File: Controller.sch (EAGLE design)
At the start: 18 parts, among them IC1 PIC16F1826/27SO, X1 057-010-1

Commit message: Updates
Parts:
- added C3: (no value), resistor:C-EUC1206
- renumbered JP1 to CS0, JP2 to CS1, JP3 to CS2, JP4 to CS3
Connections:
- net +5V: now also C3.1
- net GND: now also C3.2
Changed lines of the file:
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@@
 <part name="SUPPLY1" library="supply2" deviceset="GND" device=""/>
 <part name="SUPPLY2" library="supply2" deviceset="+5V" device=""/>
-<part name="JP1" library="SparkFun-Jumpers" deviceset="JUMPER-SMT_2_NO" device="_SILK"/>
-<part name="JP2" library="SparkFun-Jumpers" deviceset="JUMPER-SMT_2_NO" device="_SILK"/>
-<part name="JP3" library="SparkFun-Jumpers" deviceset="JUMPER-SMT_2_NO" device="_SILK"/>
-<part name="JP4" library="SparkFun-Jumpers" deviceset="JUMPER-SMT_2_NO" device="_SILK"/>
+<part name="CS0" library="SparkFun-Jumpers" deviceset="JUMPER-SMT_2_NO" device="_SILK"/>
+<part name="CS1" library="SparkFun-Jumpers" deviceset="JUMPER-SMT_2_NO" device="_SILK"/>
+<part name="CS2" library="SparkFun-Jumpers" deviceset="JUMPER-SMT_2_NO" device="_SILK"/>
+<part name="CS3" library="SparkFun-Jumpers" deviceset="JUMPER-SMT_2_NO" device="_SILK"/>
 <part name="Q1" library="crystal" deviceset="CRYSTAL" device="HC49S"/>
 <part name="C1" library="resistor" deviceset="C-EU" device="C1206"/>
@@
 <part name="SUPPLY14" library="supply2" deviceset="GND" device=""/>
 <part name="SUPPLY15" library="supply2" deviceset="+5V" device=""/>
+<part name="SUPPLY16" library="supply2" deviceset="+5V" device=""/>
+<part name="SUPPLY17" library="supply2" deviceset="GND" device=""/>
+<part name="C3" library="resistor" deviceset="C-EU" device="C1206"/>
 </parts>
 <sheets>
@@
 <instance part="SUPPLY1" gate="GND" x="35.56" y="116.84"/>
 <instance part="SUPPLY2" gate="+5V" x="58.42" y="111.76"/>
-<instance part="JP1" gate="G$1" x="109.22" y="83.82"/>
-<instance part="JP2" gate="G$1" x="109.22" y="73.66"/>
-<instance part="JP3" gate="G$1" x="109.22" y="63.5"/>
-<instance part="JP4" gate="G$1" x="109.22" y="53.34"/>
+<instance part="CS0" gate="G$1" x="109.22" y="83.82"/>
+<instance part="CS1" gate="G$1" x="109.22" y="73.66"/>
+<instance part="CS2" gate="G$1" x="109.22" y="63.5"/>
+<instance part="CS3" gate="G$1" x="109.22" y="53.34"/>
 <instance part="Q1" gate="G$1" x="76.2" y="60.96" rot="R90"/>
 <instance part="C1" gate="G$1" x="76.2" y="55.88"/>
@@
 <instance part="SUPPLY14" gate="GND" x="-12.7" y="15.24"/>
 <instance part="SUPPLY15" gate="+5V" x="-12.7" y="38.1"/>
+<instance part="SUPPLY16" gate="+5V" x="10.16" y="83.82"/>
+<instance part="SUPPLY17" gate="GND" x="10.16" y="71.12"/>
+<instance part="C3" gate="G$1" x="10.16" y="78.74"/>
 </instances>
 <busses>
@@
 <pinref part="SUPPLY14" gate="GND" pin="GND"/>
 </segment>
+<segment>
+<pinref part="SUPPLY17" gate="GND" pin="GND"/>
+<pinref part="C3" gate="G$1" pin="2"/>
+</segment>
 </net>
 <net name="+5V" class="0">
@@
 <pinref part="SUPPLY15" gate="+5V" pin="+5V"/>
 </segment>
+<segment>
+<pinref part="SUPPLY16" gate="+5V" pin="+5V"/>
+<pinref part="C3" gate="G$1" pin="1"/>
+</segment>
 </net>
 <net name="N$1" class="0">
@@
 <net name="N$4" class="0">
 <segment>
-<pinref part="JP1" gate="G$1" pin="1"/>
-<pinref part="JP2" gate="G$1" pin="1"/>
+<pinref part="CS0" gate="G$1" pin="1"/>
+<pinref part="CS1" gate="G$1" pin="1"/>
 <wire x1="104.14" y1="83.82" x2="104.14" y2="73.66" width="0.1524" layer="91"/>
-<pinref part="JP3" gate="G$1" pin="1"/>
+<pinref part="CS2" gate="G$1" pin="1"/>
 <wire x1="104.14" y1="73.66" x2="104.14" y2="63.5" width="0.1524" layer="91"/>
 <junction x="104.14" y="73.66"/>
-<pinref part="JP4" gate="G$1" pin="1"/>
+<pinref part="CS3" gate="G$1" pin="1"/>
 <wire x1="104.14" y1="63.5" x2="104.14" y2="53.34" width="0.1524" layer="91"/>
 <junction x="104.14" y="63.5"/>
@@
 <net name="N$5" class="0">
 <segment>
-<pinref part="JP1" gate="G$1" pin="2"/>
+<pinref part="CS0" gate="G$1" pin="2"/>
 <pinref part="X1" gate="-2" pin="S"/>
 </segment>
@@
 <net name="N$6" class="0">
 <segment>
-<pinref part="JP2" gate="G$1" pin="2"/>
+<pinref part="CS1" gate="G$1" pin="2"/>
 <pinref part="X1" gate="-4" pin="S"/>
 </segment>
@@
 <net name="N$7" class="0">
 <segment>
-<pinref part="JP3" gate="G$1" pin="2"/>
+<pinref part="CS2" gate="G$1" pin="2"/>
 <pinref part="X1" gate="-8" pin="S"/>
 </segment>
@@
 <net name="N$8" class="0">
 <segment>
-<pinref part="JP4" gate="G$1" pin="2"/>
+<pinref part="CS3" gate="G$1" pin="2"/>
 <pinref part="X1" gate="-10" pin="S"/>
 </segment>

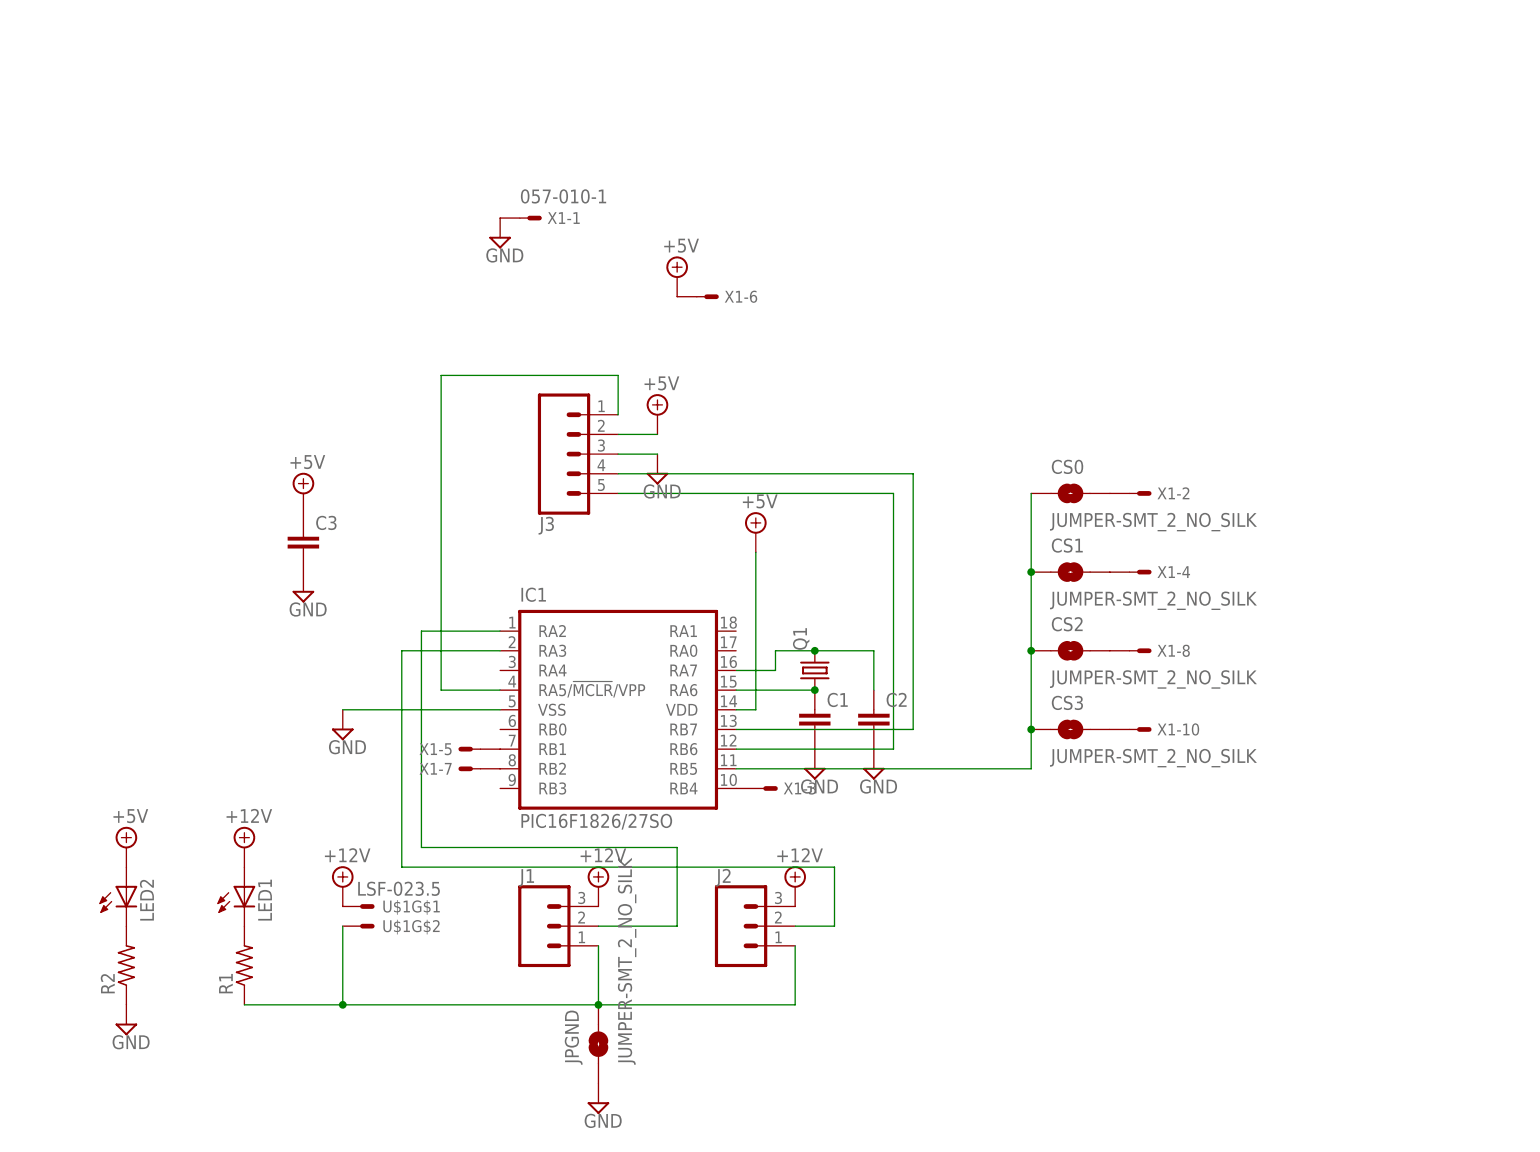
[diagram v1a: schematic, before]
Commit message: Updated design to include 5V power supply
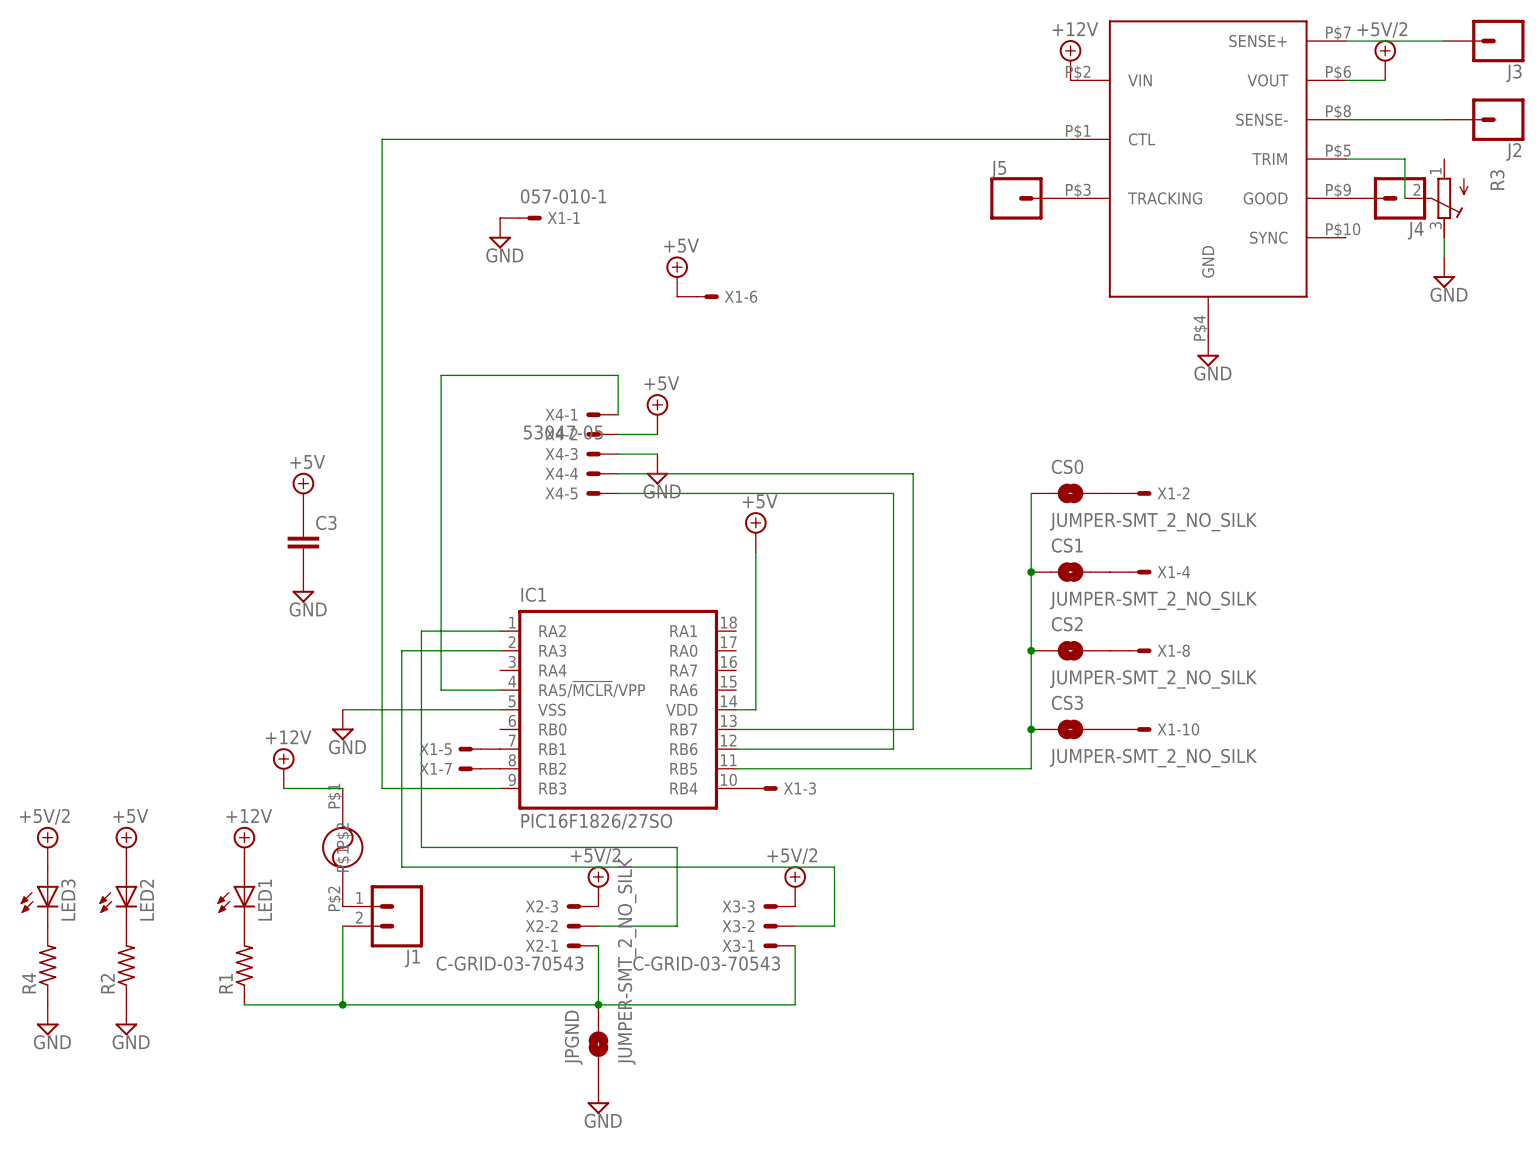
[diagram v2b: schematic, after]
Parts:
- removed C1, C2: (no value), resistor:C-EUC1206
- removed Q1: (no value), crystal:CRYSTALHC49S
- removed U$1: LSF-023.5, FRC696:LSF-023.5
- added J4, J5: (no value), SparkFun-Connectors:CONN_01
- added LED3: (no value), led:LEDCHIPLED_1206
- added R3: (no value), resistor:R-TRIMM4G/J
- added R4: (no value), resistor:R-US_R1206
- added U$2: OKL2-T12-W12, FRC696:OKL2-T12-W12
- added U$3: 0034.6081, JSB2:0034.6081
- added X2, X3: C-GRID-03-70543, con-molex:C-GRID-03-70543
- added X4: 53047-05, con-molex:53047-05
- J1: device SparkFun-Connectors:CONN_03 -> SparkFun-Connectors:CONN_023.5MM
- J2: device SparkFun-Connectors:CONN_03 -> SparkFun-Connectors:CONN_01
- J3: device SparkFun-Connectors:CONN_05 -> SparkFun-Connectors:CONN_01
- LED1, LED2: device led:LED3MM -> led:LEDCHIPLED_1206
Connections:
- new net +5V/2: LED3.A, U$2.VOUT, X2-3.S, X3-3.S
- new net N$19: R3.S, U$2.TRIM
- new net N$20: J2.1, U$2.SENSE-
- new net N$21: J3.1, U$2.SENSE+
- new net N$22: J4.1, U$2.GOOD
- new net N$23: IC1.RB3, U$2.CTL
- new net N$24: J5.1, U$2.TRACKING
- net +12V: now also U$2.VIN, U$3.P$1; no longer J1.3, J2.3, U$1G$1.S
- net +5V: now also X4-2.S; no longer J3.2
- net GND: now also R3.E, R4.1, U$2.GND, X4-3.S; no longer C1.2, C2.2, J3.3
- net N$10: now also LED3.C, R4.2; no longer C2.1, IC1.RA7, Q1.2
- net N$11: now also J1.2, X2-1.S, X3-1.S; no longer J1.1, J2.1, U$1G$2.S
- net N$12: now also X2-2.S; no longer J1.2
- net N$13: now also X3-2.S; no longer J2.2
- net N$14: now also X4-1.S; no longer J3.1
- net N$15: now also X4-4.S; no longer J3.4
- net N$16: now also X4-5.S; no longer J3.5
- net N$9: now also J1.1, U$3.P$2; no longer C1.1, IC1.RA6, Q1.1

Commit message: Removing onboard voltage regulator
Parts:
- removed J2, J3, J4, J5: (no value), SparkFun-Connectors:CONN_01
- removed LED1: (no value), led:LEDCHIPLED_1206
- removed R1: (no value), resistor:R-US_R1206
- removed R3: (no value), resistor:R-TRIMM4G/J
- removed U$2: OKL2-T12-W12, FRC696:OKL2-T12-W12
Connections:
- removed net +12V: LED1.A, U$2.VIN, U$3.P$1
- removed net N$17: LED1.C, R1.2
- removed net N$19: R3.S, U$2.TRIM
- removed net N$20: J2.1, U$2.SENSE-
- removed net N$21: J3.1, U$2.SENSE+
- removed net N$22: J4.1, U$2.GOOD
- removed net N$23: IC1.RB3, U$2.CTL
- removed net N$24: J5.1, U$2.TRACKING
- net +5V/2: now also U$3.P$1; no longer U$2.VOUT
- net GND: no longer R3.E, U$2.GND
- net N$11: no longer R1.1
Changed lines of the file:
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@@
 <part name="SUPPLY9" library="supply2" deviceset="+5V" device=""/>
 <part name="SUPPLY10" library="supply2" deviceset="GND" device=""/>
-<part name="LED1" library="led" deviceset="LED" device="CHIPLED_1206"/>
-<part name="R1" library="resistor" deviceset="R-US_" device="R1206"/>
-<part name="SUPPLY13" library="supply2" deviceset="+12V" device=""/>
 <part name="LED2" library="led" deviceset="LED" device="CHIPLED_1206"/>
 <part name="R2" library="resistor" deviceset="R-US_" device="R1206"/>
@@
 <part name="SUPPLY7" library="supply2" deviceset="+5V/2" device=""/>
 <part name="SUPPLY8" library="supply2" deviceset="+5V/2" device=""/>
-<part name="U$2" library="FRC696" deviceset="OKL2-T12-W12" device=""/>
-<part name="SUPPLY18" library="supply2" deviceset="GND" device=""/>
-<part name="SUPPLY19" library="supply2" deviceset="+12V" device=""/>
-<part name="SUPPLY20" library="supply2" deviceset="+5V/2" device=""/>
-<part name="R3" library="resistor" deviceset="R-TRIMM" device="4G/J"/>
-<part name="SUPPLY21" library="supply2" deviceset="GND" device=""/>
 <part name="X2" library="con-molex" deviceset="C-GRID-03" device="-70543"/>
 <part name="X3" library="con-molex" deviceset="C-GRID-03" device="-70543"/>
@@
 <part name="U$3" library="JSB2" deviceset="0034.6081" device=""/>
 <part name="J1" library="SparkFun-Connectors" deviceset="CONN_02" device="3.5MM"/>
-<part name="SUPPLY3" library="supply2" deviceset="+12V" device=""/>
 <part name="LED3" library="led" deviceset="LED" device="CHIPLED_1206"/>
 <part name="R4" library="resistor" deviceset="R-US_" device="R1206"/>
 <part name="SUPPLY4" library="supply2" deviceset="GND" device=""/>
 <part name="SUPPLY11" library="supply2" deviceset="+5V/2" device=""/>
-<part name="J2" library="SparkFun-Connectors" deviceset="CONN_01" device=""/>
-<part name="J3" library="SparkFun-Connectors" deviceset="CONN_01" device=""/>
-<part name="J4" library="SparkFun-Connectors" deviceset="CONN_01" device=""/>
-<part name="J5" library="SparkFun-Connectors" deviceset="CONN_01" device=""/>
+<part name="SUPPLY3" library="supply2" deviceset="+5V/2" device=""/>
 </parts>
 <sheets>
@@
 <instance part="SUPPLY9" gate="+5V" x="55.88" y="93.98"/>
 <instance part="SUPPLY10" gate="GND" x="55.88" y="86.36"/>
-<instance part="LED1" gate="G$1" x="2.54" y="33.02"/>
-<instance part="R1" gate="G$1" x="2.54" y="22.86" rot="R90"/>
-<instance part="SUPPLY13" gate="+12V" x="2.54" y="38.1"/>
 <instance part="LED2" gate="G$1" x="-12.7" y="33.02"/>
 <instance part="R2" gate="G$1" x="-12.7" y="22.86" rot="R90"/>
@@
 <instance part="SUPPLY7" gate="G$1" x="48.26" y="33.02"/>
 <instance part="SUPPLY8" gate="G$1" x="73.66" y="33.02"/>
-<instance part="U$2" gate="G$1" x="129.54" y="121.92"/>
-<instance part="SUPPLY18" gate="GND" x="127" y="101.6"/>
-<instance part="SUPPLY19" gate="+12V" x="7.62" y="48.26"/>
-<instance part="SUPPLY20" gate="G$1" x="149.86" y="139.7"/>
-<instance part="R3" gate="G$1" x="157.48" y="121.92" rot="R180"/>
-<instance part="SUPPLY21" gate="GND" x="157.48" y="111.76"/>
 <instance part="X2" gate="-1" x="45.72" y="25.4" rot="R180"/>
 <instance part="X2" gate="-2" x="45.72" y="27.94" rot="R180"/>
@@
 <instance part="U$3" gate="G$1" x="15.24" y="38.1" rot="R270"/>
 <instance part="J1" gate="G$1" x="22.86" y="30.48" rot="R180"/>
-<instance part="SUPPLY3" gate="+12V" x="109.22" y="139.7"/>
 <instance part="LED3" gate="G$1" x="-22.86" y="33.02"/>
 <instance part="R4" gate="G$1" x="-22.86" y="22.86" rot="R90"/>
 <instance part="SUPPLY4" gate="GND" x="-22.86" y="15.24"/>
 <instance part="SUPPLY11" gate="G$1" x="-22.86" y="38.1"/>
-<instance part="J2" gate="G$1" x="165.1" y="132.08" rot="R180"/>
-<instance part="J3" gate="G$1" x="165.1" y="142.24" rot="R180"/>
-<instance part="J4" gate="G$1" x="152.4" y="121.92" rot="R180"/>
-<instance part="J5" gate="G$1" x="101.6" y="121.92"/>
+<instance part="SUPPLY3" gate="G$1" x="7.62" y="48.26"/>
 </instances>
 <busses>
@@
 <pinref part="SUPPLY17" gate="GND" pin="GND"/>
 <pinref part="C3" gate="G$1" pin="2"/>
-</segment>
-<segment>
-<pinref part="U$2" gate="G$1" pin="GND"/>
-<pinref part="SUPPLY18" gate="GND" pin="GND"/>
-</segment>
-<segment>
-<pinref part="R3" gate="G$1" pin="E"/>
-<pinref part="SUPPLY21" gate="GND" pin="GND"/>
-<wire x1="157.48" y1="114.3" x2="157.48" y2="116.84" width="0.1524" layer="91"/>
 </segment>
 <segment>
@@
 </segment>
 </net>
-<net name="+12V" class="0">
-<segment>
-<pinref part="SUPPLY13" gate="+12V" pin="+12V"/>
-<pinref part="LED1" gate="G$1" pin="A"/>
-</segment>
-<segment>
-<pinref part="U$3" gate="G$1" pin="P$1"/>
-<pinref part="SUPPLY19" gate="+12V" pin="+12V"/>
-<wire x1="7.62" y1="45.72" x2="15.24" y2="45.72" width="0.1524" layer="91"/>
-</segment>
-<segment>
-<pinref part="U$2" gate="G$1" pin="VIN"/>
-<pinref part="SUPPLY3" gate="+12V" pin="+12V"/>
-</segment>
-</net>
 <net name="N$11" class="0">
 <segment>
@@
 <wire x1="48.26" y1="17.78" x2="73.66" y2="17.78" width="0.1524" layer="91"/>
 <pinref part="JPGND" gate="G$1" pin="2"/>
-<pinref part="R1" gate="G$1" pin="1"/>
-<wire x1="2.54" y1="17.78" x2="15.24" y2="17.78" width="0.1524" layer="91"/>
-<junction x="15.24" y="17.78"/>
 <pinref part="X2" gate="-1" pin="S"/>
 <pinref part="X3" gate="-1" pin="S"/>
@@
 </segment>
 </net>
-<net name="N$17" class="0">
-<segment>
-<pinref part="LED1" gate="G$1" pin="C"/>
-<pinref part="R1" gate="G$1" pin="2"/>
-</segment>
-</net>
 <net name="N$18" class="0">
 <segment>
@@
 <net name="+5V/2" class="0">
 <segment>
-<pinref part="U$2" gate="G$1" pin="VOUT"/>
-<pinref part="SUPPLY20" gate="G$1" pin="+5V/2"/>
-<wire x1="144.78" y1="137.16" x2="149.86" y2="137.16" width="0.1524" layer="91"/>
-</segment>
-<segment>
 <pinref part="SUPPLY7" gate="G$1" pin="+5V/2"/>
 <pinref part="X2" gate="-3" pin="S"/>
@@
 <pinref part="SUPPLY11" gate="G$1" pin="+5V/2"/>
 </segment>
-</net>
-<net name="N$19" class="0">
-<segment>
-<pinref part="U$2" gate="G$1" pin="TRIM"/>
-<pinref part="R3" gate="G$1" pin="S"/>
-<wire x1="144.78" y1="127" x2="152.4" y2="127" width="0.1524" layer="91"/>
-<wire x1="152.4" y1="127" x2="152.4" y2="121.92" width="0.1524" layer="91"/>
+<segment>
+<pinref part="U$3" gate="G$1" pin="P$1"/>
+<wire x1="7.62" y1="45.72" x2="15.24" y2="45.72" width="0.1524" layer="91"/>
+<pinref part="SUPPLY3" gate="G$1" pin="+5V/2"/>
 </segment>
 </net>
@@
 </segment>
 </net>
-<net name="N$20" class="0">
-<segment>
-<pinref part="U$2" gate="G$1" pin="SENSE-"/>
-<pinref part="J2" gate="G$1" pin="1"/>
-<wire x1="144.78" y1="132.08" x2="157.48" y2="132.08" width="0.1524" layer="91"/>
-</segment>
-</net>
-<net name="N$21" class="0">
-<segment>
-<pinref part="J3" gate="G$1" pin="1"/>
-<pinref part="U$2" gate="G$1" pin="SENSE+"/>
-<wire x1="157.48" y1="142.24" x2="144.78" y2="142.24" width="0.1524" layer="91"/>
-</segment>
-</net>
-<net name="N$22" class="0">
-<segment>
-<pinref part="U$2" gate="G$1" pin="GOOD"/>
-<pinref part="J4" gate="G$1" pin="1"/>
-</segment>
-</net>
-<net name="N$23" class="0">
-<segment>
-<pinref part="IC1" gate="G$1" pin="RB3"/>
-<wire x1="35.56" y1="45.72" x2="20.32" y2="45.72" width="0.1524" layer="91"/>
-<wire x1="20.32" y1="45.72" x2="20.32" y2="129.54" width="0.1524" layer="91"/>
-<pinref part="U$2" gate="G$1" pin="CTL"/>
-<wire x1="20.32" y1="129.54" x2="109.22" y2="129.54" width="0.1524" layer="91"/>
-</segment>
-</net>
-<net name="N$24" class="0">
-<segment>
-<pinref part="U$2" gate="G$1" pin="TRACKING"/>
-<pinref part="J5" gate="G$1" pin="1"/>
-</segment>
-</net>
